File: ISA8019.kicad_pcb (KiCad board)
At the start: 2 copper layers, 157.4 x 74.2 mm, 56 parts, among them J1 Bus_ISA_16bit, J2 8P8C_Shielded, J4 Jumper mode, J5 PNP force, J6 BROM size and base address, J7 I/O base address, J8 Medium type, J9 IRQ select, T1 13F-39MNL, U1 RTL8019AS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

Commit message: 8 bit network card variant
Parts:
- removed H2: MountingHole, ToolingHole:ToolingHole_JLCSMT
- J1: value Bus_ISA_16bit -> Bus_ISA_8bit; footprint Bus_AT_without_Silkscreen:BUS_AT_WO_SILKSCREEN -> My_Components:Conn_Edge_PCB_ISA8
- moved J1 38.1 mm to (129.6, 159.3)
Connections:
- J1 pad 15: Net-(J1-Pad15) -> (no net)
- J1 pad 16: Net-(J1-Pad16) -> (no net)
- J1 pad 17: Net-(J1-Pad17) -> (no net)
- J1 pad 18: Net-(J1-Pad18) -> (no net)
- J1 pad 19: Net-(J1-Pad19) -> (no net)
- J1 pad 20: Net-(J1-Pad20) -> (no net)
- J1 pad 21: /ISA_IRQ7 -> (no net)
- J1 pad 22: /ISA_IRQ6 -> (no net)
- J1 pad 26: Net-(J1-Pad26) -> (no net)
- J1 pad 27: Net-(J1-Pad27) -> (no net)
- J1 pad 28: Net-(J1-Pad28) -> (no net)
- J1 pad 30: Net-(J1-Pad30) -> (no net)
- J1 pad 32: Net-(J1-Pad32) -> (no net)
- J1 pad 5: Net-(J1-Pad5) -> (no net)
- J1 pad 6: Net-(J1-Pad6) -> (no net)
- J1 pad 7: Net-(J1-Pad7) -> (no net)
- J1 pad 8: Net-(J1-Pad8) -> (no net)
- J1 pad 9: +12V -> (no net)
- J2 pad 4: Net-(J2-Pad4) -> (no net)
- J2 pad 5: Net-(J2-Pad5) -> (no net)
- J2 pad 7: Net-(J2-Pad7) -> (no net)
- J2 pad 8: Net-(J2-Pad8) -> (no net)
- U1 pad 100: /ISA_IRQ10 -> (no net)
- U1 pad 48: /TX- -> (no net)
- U1 pad 49: /TX+ -> (no net)
- U1 pad 53: /CD- -> (no net)
- U1 pad 54: /CD+ -> (no net)
- U1 pad 55: /RX- -> (no net)
- U1 pad 56: /RX+ -> (no net)
- U1 pad 60: /LEDBNC -> (no net)
- U1 pad 63: /LED2 -> (no net)
- U1 pad 87: /ISA_D15 -> (no net)
- U1 pad 88: /ISA_D14 -> (no net)
- U1 pad 90: /ISA_D13 -> (no net)
- U1 pad 91: /ISA_D12 -> (no net)
- U1 pad 92: /ISA_D11 -> (no net)
- U1 pad 93: /ISA_D10 -> (no net)
- U1 pad 94: /ISA_D9 -> (no net)
- U1 pad 95: /ISA_D8 -> (no net)
- U1 pad 97: /ISA_IRQ15 -> (no net)
- U1 pad 98: /ISA_IRQ12 -> (no net)
- U1 pad 99: /ISA_IRQ11 -> (no net)
- U2 pad 7: Net-(U2-Pad7) -> (no net)
- U3 pad 1: Net-(U3-Pad1) -> (no net)
- U3 pad 30: Net-(U3-Pad30) -> (no net)
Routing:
- net /ISA_D15: track 87.1 -> 0.00 mm
- net /ISA_D14: track 84.3 -> 0.00 mm
- net /ISA_D13: track 81.2 -> 0.00 mm
- net /ISA_D12: track 78.4 -> 0.00 mm
- net /ISA_D11: track 75.6 -> 0.00 mm
- net /ISA_D10: track 72.8 -> 0.00 mm
- net /ISA_D9: track 70.0 -> 0.00 mm
- net /ISA_D8: track 67.2 -> 0.00 mm
- net /ISA_IRQ15: track 53.9 -> 0.00 mm, vias 1 -> 0
- net /ISA_IRQ12: track 51.1 -> 0.00 mm, vias 1 -> 0
- net /ISA_IRQ11: track 48.3 -> 0.00 mm, vias 1 -> 0
- net /~ISA_IOCS16: track 50.7 -> 2.95 mm, vias 1 -> 0
- net /ISA_IRQ10: track 45.5 -> 0.00 mm, vias 1 -> 0
- net /ISA_A13: track 122.3 -> 151.6 mm
- net /BA15: track 99.2 -> 116.3 mm
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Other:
- outline, holes or cut-outs redrawn
- board text added: "Original Design by Tobias Mädel and Tobias Schramm 8-Bit variant by Hkz"
- board text removed: "Designed by Tobias Mädel and Tobias Schramm"

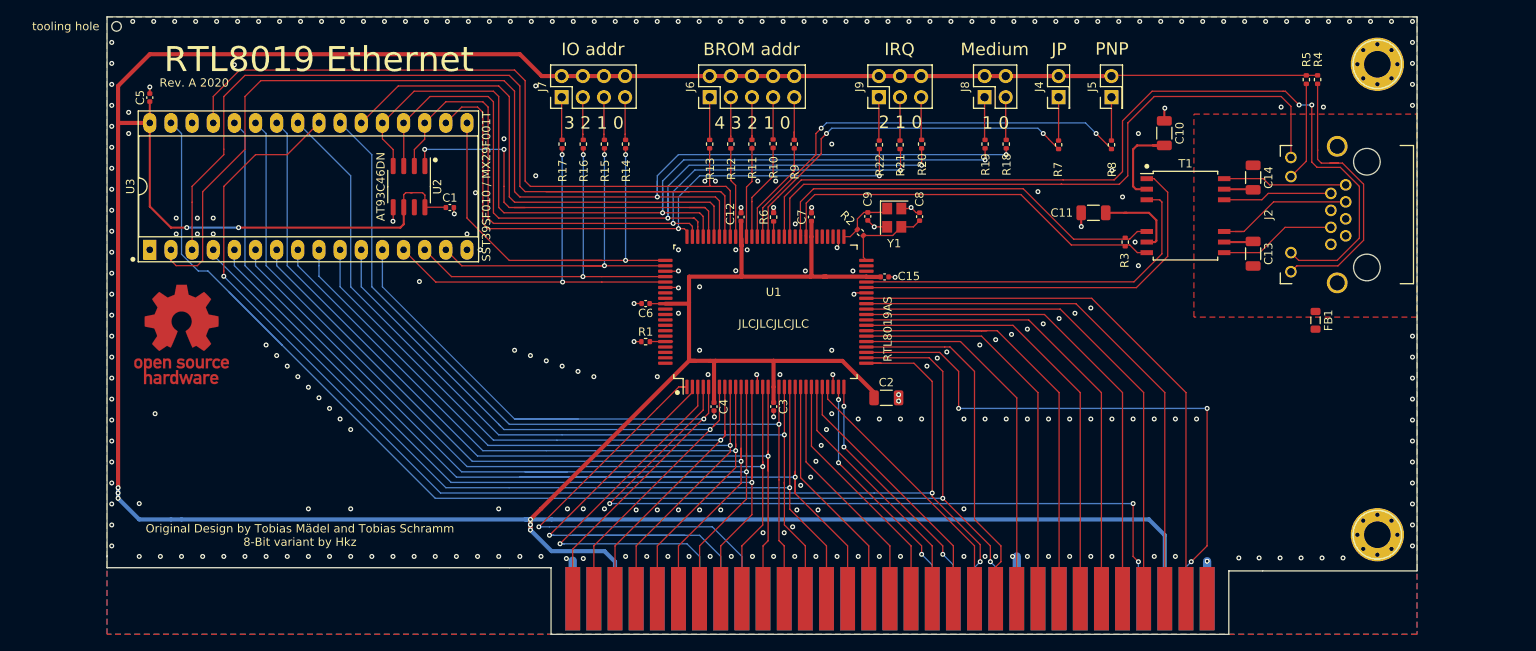
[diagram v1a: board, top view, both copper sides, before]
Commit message: Redraw 8 bit board
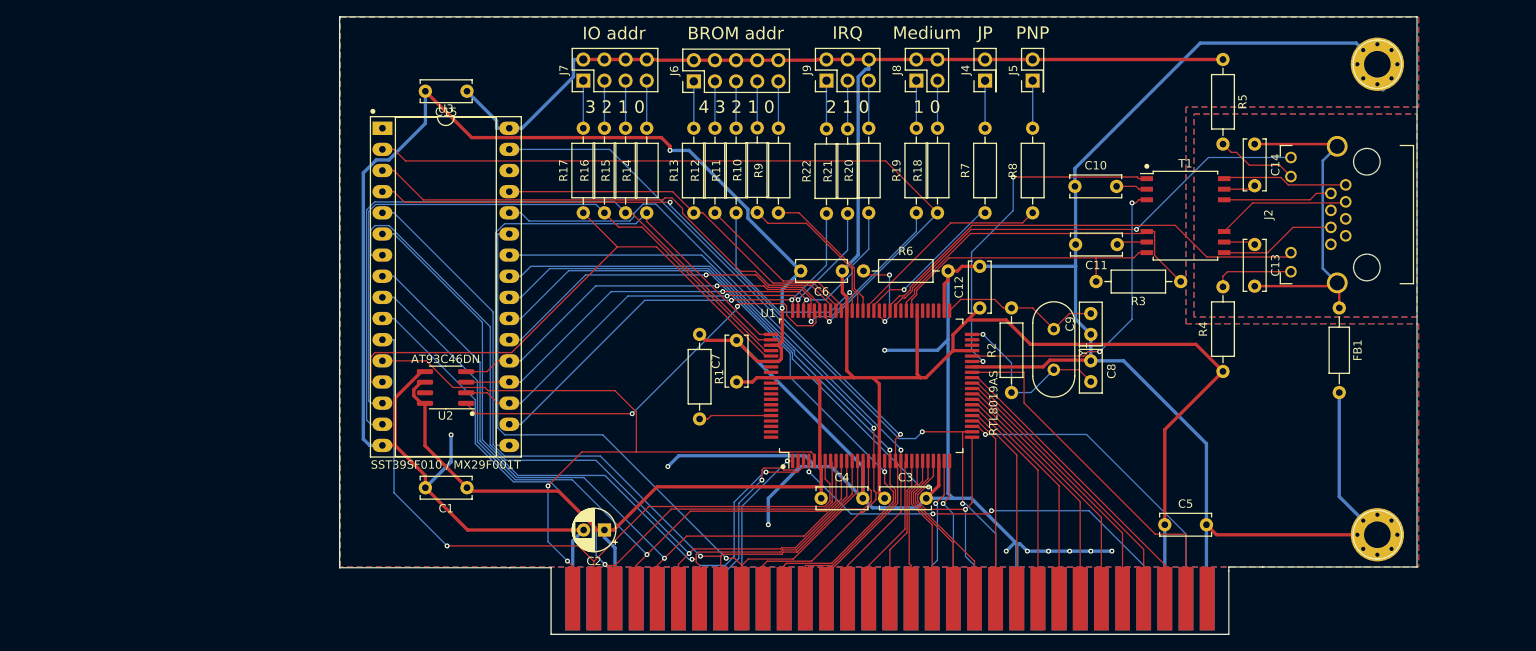
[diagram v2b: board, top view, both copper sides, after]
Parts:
- removed H1: MountingHole, ToolingHole:ToolingHole_JLCSMT
- removed H5: OSHW Logo, Symbol:OSHW-Logo_11.4x12mm_Copper
- C1, C12, C15, C3, C4, C5, C6, C7: footprint Capacitor_SMD:C_0402_1005Metric -> Capacitor_THT:C_Disc_D6.0mm_W2.5mm_P5.00mm
- C10, C11, C13, C14: footprint Capacitor_SMD:C_1206_3216Metric -> Capacitor_THT:C_Disc_D6.0mm_W2.5mm_P5.00mm
- C2: value 47µF 10V -> 47uF; footprint Capacitor_SMD:C_1206_3216Metric -> Capacitor_THT:CP_Radial_D5.0mm_P2.50mm
- C8, C9: footprint Capacitor_SMD:C_0402_1005Metric -> Capacitor_THT:C_Disc_D5.0mm_W2.5mm_P2.50mm
- FB1: footprint Inductor_SMD:L_0805_2012Metric -> Inductor_THT:L_Axial_L5.3mm_D2.2mm_P10.16mm_Horizontal_Vishay_IM-1
- R1, R10, R11, R12, R13, R14, R15, R16, R17, R18, R19, R2, R20, R21, R22, R3, R4, R5, R6, R7, R8, R9: footprint Resistor_SMD:R_0402_1005Metric -> Resistor_THT:R_Axial_DIN0207_L6.3mm_D2.5mm_P10.16mm_Horizontal
- Y1: value 20MHz -> 20Mhz; footprint Crystal:Crystal_SMD_3225-4Pin_3.2x2.5mm -> Crystal:Crystal_HC49-4H_Vertical
- moved C5 132.3 mm to (162.6, 150.4), turned to 0 degrees
- moved C15 54.9 mm to (78.8, 98.3), turned to 180 degrees
- moved C2 37.4 mm to (95.3, 151.0), turned to 180 degrees
- moved R4 36.8 mm to (169.6, 132.0), turned to 90 degrees
- moved C1 33.7 mm to (78.8, 146.0), turned to 180 degrees
- moved U3 31.5 mm to (68.6, 102.8), turned to 0 degrees
- moved C12 30.7 mm to (140.4, 124.4)
- moved C9 30.3 mm to (153.7, 127.5)
- moved C8 26.9 mm to (153.7, 130.7)
- moved R2 26.4 mm to (144.2, 134.5), turned to 90 degrees
- moved U2 24.5 mm to (76.2, 133.9), turned to 180 degrees
- moved C6 23.9 mm to (123.9, 119.9)
- moved Y1 23.4 mm to (149.3, 126.9)
- moved C7 21.8 mm to (111.2, 133.3)
- moved C3 17.3 mm to (129.0, 147.2), turned to 0 degrees
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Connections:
- Y1 pad 2: GND -> Net-(C8-Pad2)
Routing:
- net GND: track 41.3 -> 545.4 mm, vias 289 -> 12
- net +5V: track 525.1 -> 348.0 mm, vias 8 -> 0
- net /~ISA_SMEMW: track 168.7 -> 92.2 mm
- net /ISA_A13: track 151.6 -> 81.4 mm
- net /~ISA_SMEMR: track 161.8 -> 91.9 mm, vias 3 -> 2
- net /BA14: track 150.7 -> 89.8 mm, vias 2 -> 1
- net /BA15: track 116.3 -> 61.8 mm
- net /LED1: track 107.4 -> 54.7 mm, vias 2 -> 0
- net /BA16: track 89.8 -> 45.5 mm
- net /ISA_IRQ2: track 93.5 -> 50.5 mm
- net /ISA_IRQ4: track 65.4 -> 22.9 mm
- net /BD7: track 110.6 -> 68.7 mm
- net Earth: track 0.00 -> 41.1 mm
- net /BD2: track 43.9 -> 83.2 mm, vias 2 -> 0
- net /ISA_IRQ5: track 56.2 -> 19.5 mm
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- added copper zone on B.Cu, net (none)
- added copper zone on F.Cu, net (none)
- added copper zone on B.Cu, net Earth
- removed copper zone on F.Cu, net Earth
- removed copper zone on B.Cu, net GND
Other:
- board size 157.4 x 74.2 mm -> 129.4 x 74.2 mm
- net class POWER added: clearance 0.127, trace_width 0.4, via_dia 0.6, via_drill 0.3
- board text removed: "JLCJLCJLCJLC"
- board text removed: "Original Design by Tobias Mädel and Tobias Schramm 8-Bit variant by Hkz"
- board text removed: "RTL8019 Ethernet"
- board text removed: "Rev. A 2020"
- board text removed: "tbspace.de"

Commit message: cleanup board a bit
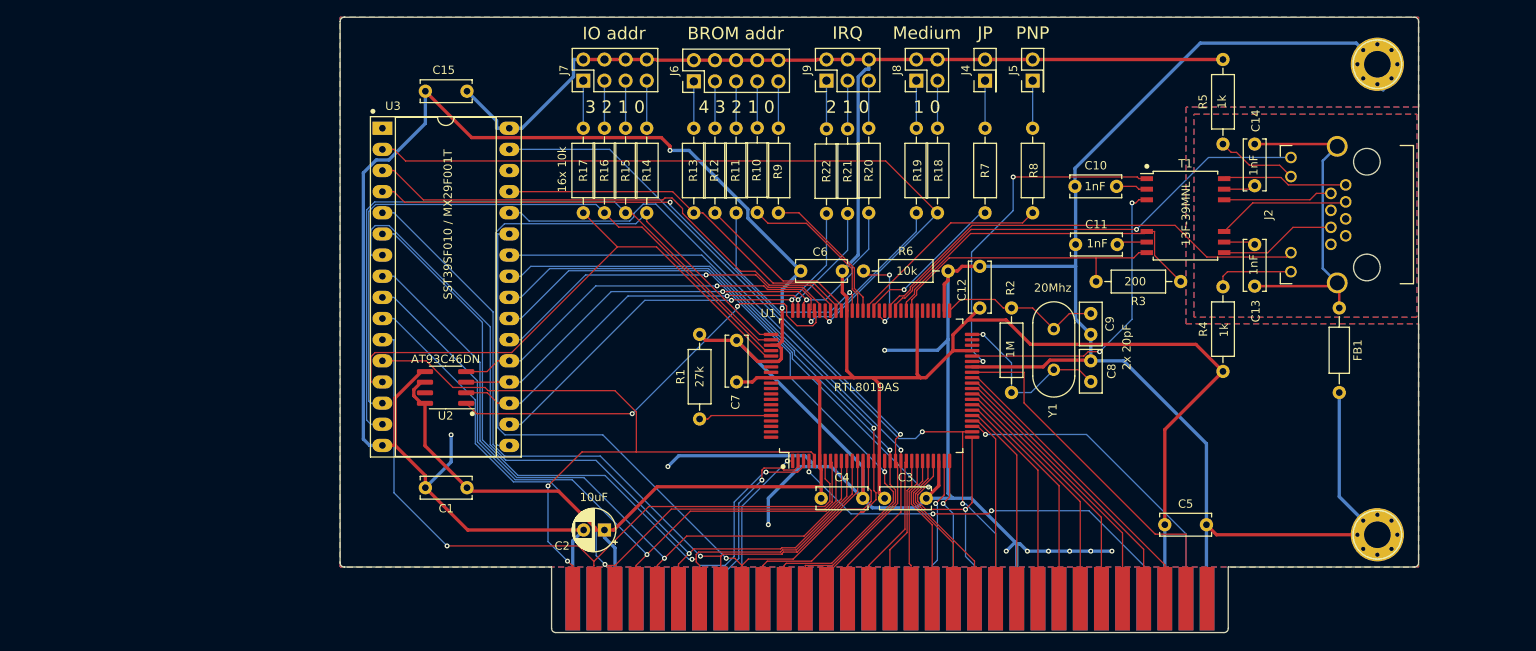
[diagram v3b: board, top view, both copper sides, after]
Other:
- board size 129.4 x 74.2 mm -> 129.5 x 73.9 mm
- board text added: "10k"
- board text added: "10uF"
- board text added: "13F-39MNL"
- board text added: "16x 10k"
- board text added: "1M"
- board text added: "1k"
- board text added: "1nF"
- board text added: "200"
- board text added: "20Mhz"
- board text added: "27k"
- board text added: "2x 20pF"

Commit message: Update board
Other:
- board text added: "RTL8019 ISA 8-Bit rev.1"
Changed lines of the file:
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@@
   (general
     (thickness 1.6)
-    (drawings 64)
+    (drawings 65)
     (tracks 938)
     (zones 0)
@@
   (page A4)
   (layers
-    (0 F.Cu signal hide)
-    (31 B.Cu signal hide)
-    (32 B.Adhes user hide)
-    (33 F.Adhes user hide)
-    (34 B.Paste user hide)
-    (35 F.Paste user hide)
+    (0 F.Cu signal)
+    (31 B.Cu signal)
+    (32 B.Adhes user)
+    (33 F.Adhes user)
+    (34 B.Paste user)
+    (35 F.Paste user)
     (36 B.SilkS user)
-    (37 F.SilkS user hide)
+    (37 F.SilkS user)
     (38 B.Mask user hide)
     (39 F.Mask user hide)
@@
     )
   )
+  (gr_text "RTL8019\nISA 8-Bit rev.1" (at 65.338 151.934) (layer F.SilkS)
+    (effects (font (size 1 1) (thickness 0.15)) (justify left))
+  )
   (gr_line (start 93.532 99.102) (end 93.532 148.632) (layer B.SilkS) (width 0.12))

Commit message: Fix top zone fill
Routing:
- added copper zone on F.Cu, net Earth
- removed copper zone on F.Cu, net (none)
